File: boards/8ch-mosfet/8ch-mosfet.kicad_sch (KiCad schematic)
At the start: 16 parts, among them J1 N2K, J2 I2C, J3 Screw_Terminal_01x08, J4 Screw_Terminal_01x08, U1 ESP32-DEVKITC, U2 MCP3208, U3 R-78B3.3-2.0

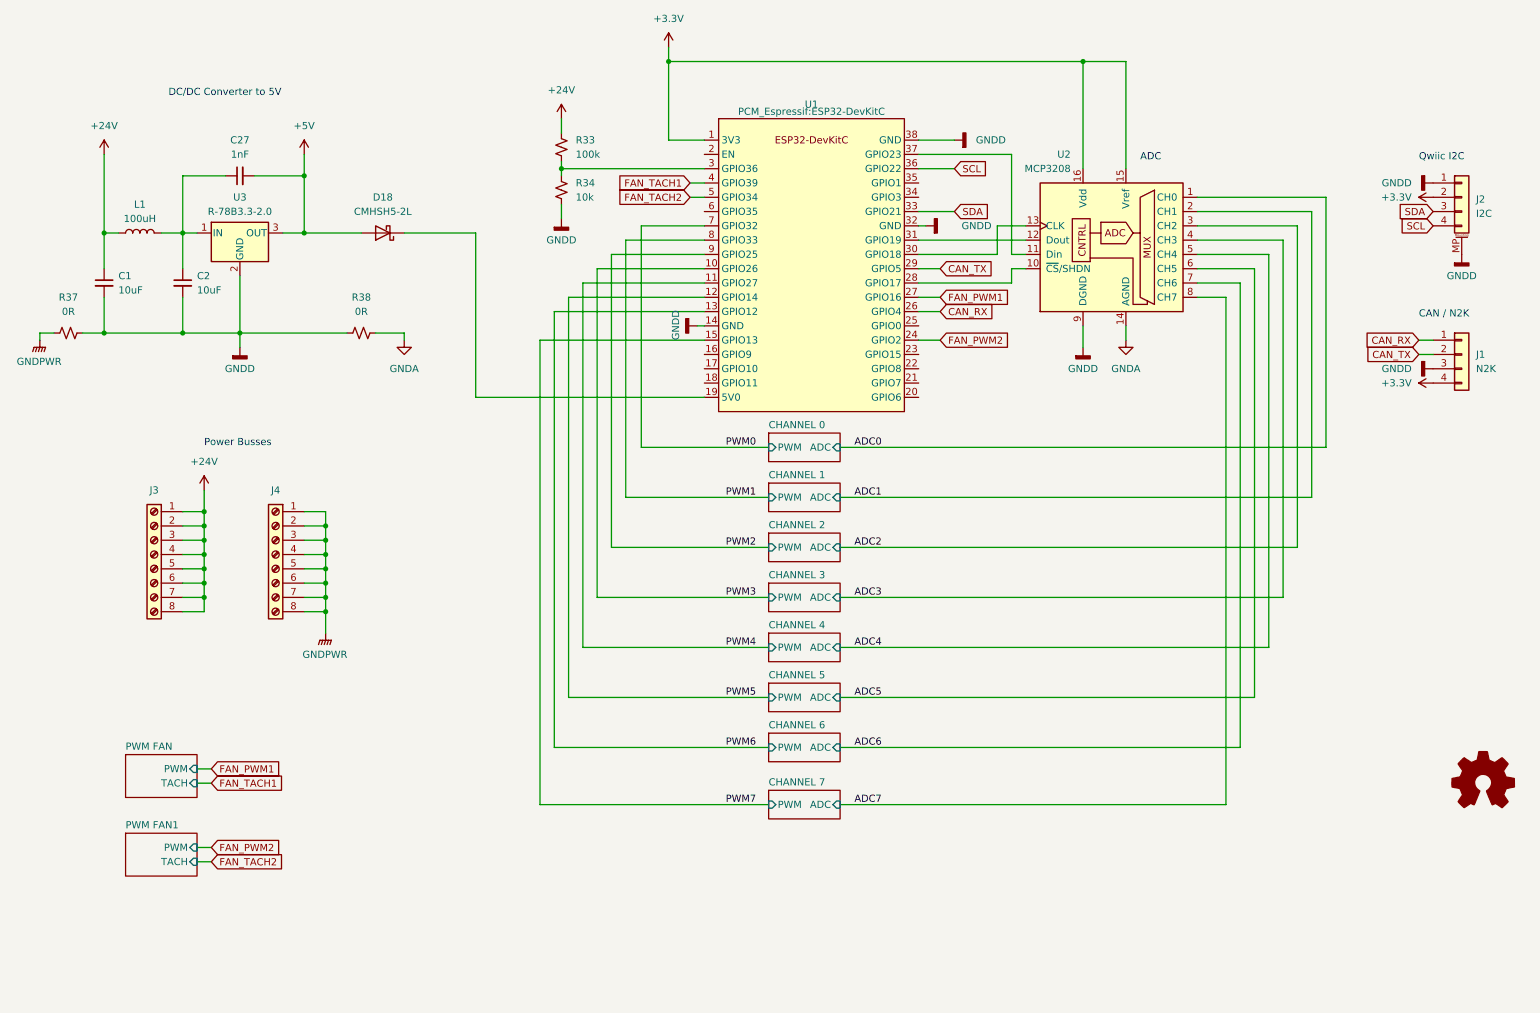
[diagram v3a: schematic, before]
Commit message: added a better adc for getting bus voltage
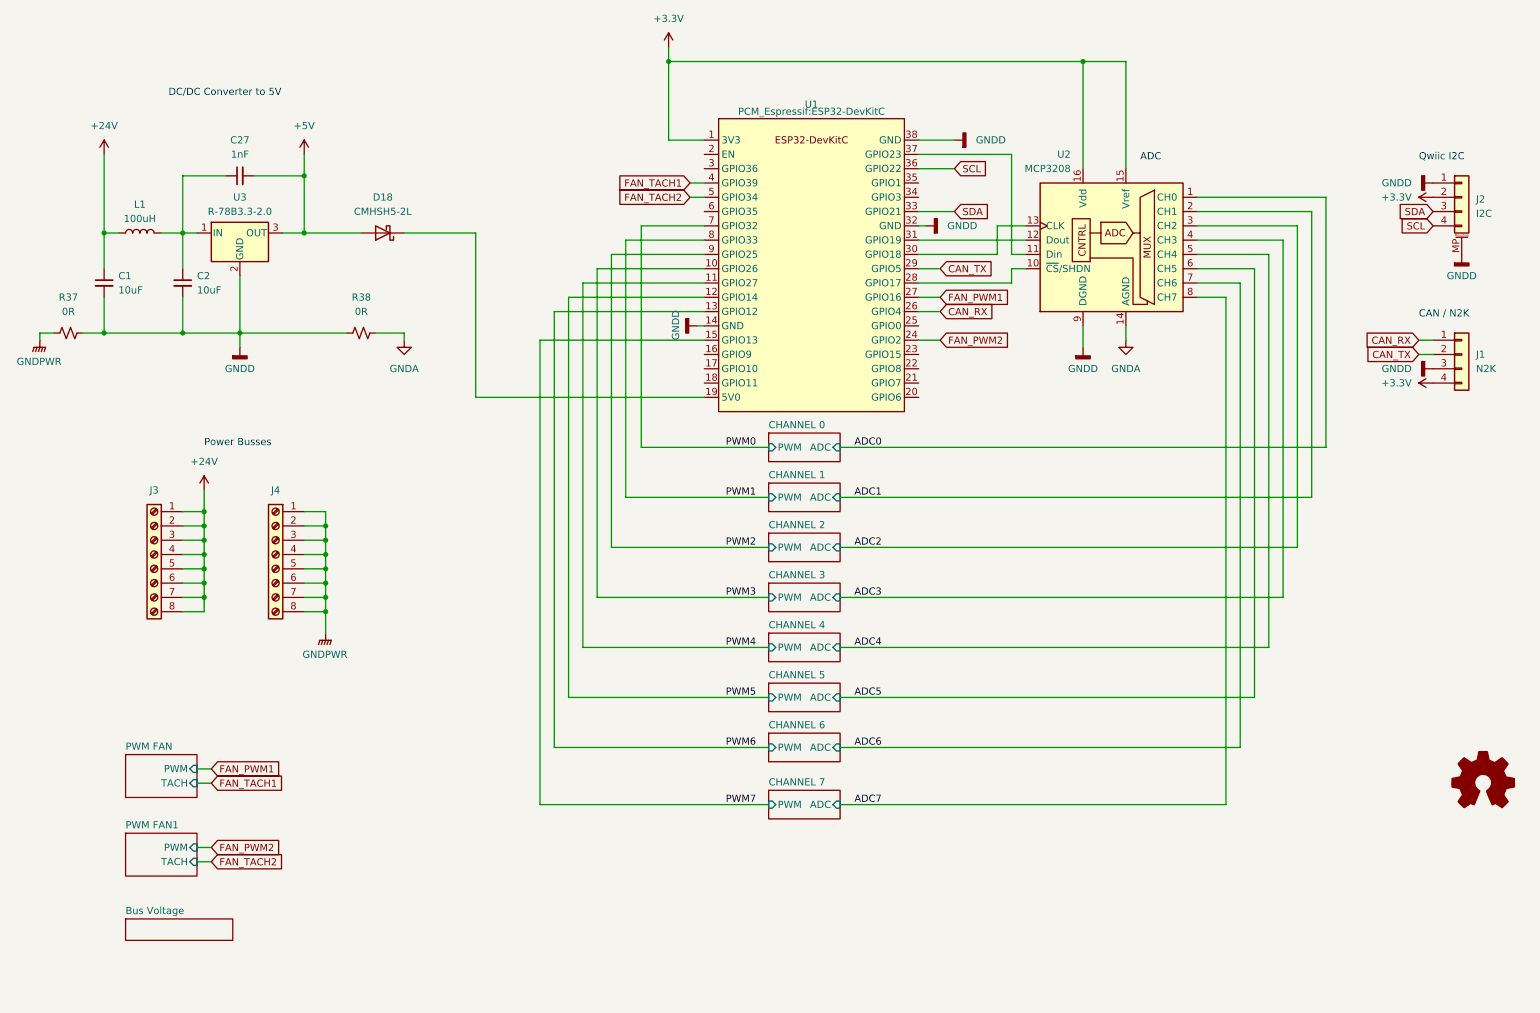
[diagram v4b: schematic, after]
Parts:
- removed R33: 100k, Resistor_SMD:R_0805_2012Metric_Pad1.20x1.40mm_HandSolder, symbol Device:R_Small_US
- removed R34: 10k, Resistor_SMD:R_0805_2012Metric_Pad1.20x1.40mm_HandSolder, symbol Device:R_Small_US
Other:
- added sheet Bus Voltage (bus voltage.kicad_sch)
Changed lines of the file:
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@@
   (junction (at 48.26 110.49) (diameter 0) (color 0 0 0 0)
   )
-  (junction (at 111.76 49.53) (diameter 0) (color 0 0 0 0)
-  )
   (junction (at 48.26 113.03) (diameter 0) (color 0 0 0 0)
   )
@@
     (stroke (width 0) (type default))
   )
-  (wire (pts (xy 111.76 48.26) (xy 111.76 49.53))
-    (stroke (width 0) (type default))
-  )
   (wire (pts (xy 115.57 134.62) (xy 148.59 134.62))
     (stroke (width 0) (type default))
@@
     (stroke (width 0) (type default))
   )
-  (wire (pts (xy 111.76 40.64) (xy 111.76 43.18))
-    (stroke (width 0) (type default))
-  )
   (wire (pts (xy 175.26 44.45) (xy 181.61 44.45))
     (stroke (width 0) (type default))
@@
     (stroke (width 0) (type default))
   )
-  (wire (pts (xy 111.76 49.53) (xy 111.76 50.8))
-    (stroke (width 0) (type default))
-  )
   (wire (pts (xy 48.26 113.03) (xy 48.26 115.57))
     (stroke (width 0) (type default))
@@
     (stroke (width 0) (type default))
   )
-  (wire (pts (xy 111.76 49.53) (xy 137.16 49.53))
-    (stroke (width 0) (type default))
-  )
   (wire (pts (xy 175.26 80.01) (xy 179.07 80.01))
     (stroke (width 0) (type default))
@@
   )
   (wire (pts (xy 204.47 30.48) (xy 204.47 49.53))
-    (stroke (width 0) (type default))
-  )
-  (wire (pts (xy 111.76 55.88) (xy 111.76 58.42))
     (stroke (width 0) (type default))
   )
@@
       (effects (font (size 1.27 1.27)) hide)
     )
-    (property "Value" "GNDD" (at 182.88 59.69 90)
+    (property "Value" "GNDD" (at 180.34 59.69 90)
       (effects (font (size 1.27 1.27)) (justify right))
     )
@@
         (path "/c83c6236-96e9-46ad-9d7a-9e2efa4a7966/a8a81147-5613-4820-beb3-a7ca76d0db8e"
           (reference "R29") (unit 1)
-        )
-      )
-    )
-  )
-  (symbol (lib_id "Device:R_Small_US") (at 111.76 53.34 180) (unit 1)
-    (in_bom yes) (on_board yes) (dnp no) (fields_autoplaced)
-    (property "Reference" "R34" (at 114.3 52.07 0)
-      (effects (font (size 1.27 1.27)) (justify right))
-    )
-    (property "Value" "10k" (at 114.3 54.61 0)
-      (effects (font (size 1.27 1.27)) (justify right))
-    )
-    (property "Footprint" "Resistor_SMD:R_0805_2012Metric_Pad1.20x1.40mm_HandSolder" (at 111.76 53.34 0)
-      (effects (font (size 1.27 1.27)) hide)
-    )
-    (property "Datasheet" "~" (at 111.76 53.34 0)
-      (effects (font (size 1.27 1.27)) hide)
-    )
-    (property "Vendor" "652-CR0805JW-104ELF" (at 111.76 53.34 0)
-      (effects (font (size 1.27 1.27)) hide)
-    )
-    (pin "1")
-    (pin "2")
-    (instances
-      (project "8ch-mosfet"
-        (path "/c83c6236-96e9-46ad-9d7a-9e2efa4a7966"
-          (reference "R34") (unit 1)
-        )
-        (path "/c83c6236-96e9-46ad-9d7a-9e2efa4a7966/0eec6767-666b-42c0-ba36-2a83c9caeade"
-          (reference "R4") (unit 1)
-        )
-        (path "/c83c6236-96e9-46ad-9d7a-9e2efa4a7966/ccdb1c25-8d0f-4f30-ab70-bbc1ecf3f6f7"
-          (reference "R8") (unit 1)
-        )
-        (path "/c83c6236-96e9-46ad-9d7a-9e2efa4a7966/1e692482-a022-407a-8cb5-d9a3b23521a6"
-          (reference "R12") (unit 1)
-        )
-        (path "/c83c6236-96e9-46ad-9d7a-9e2efa4a7966/5952e660-2bb6-45cf-b9ea-f7a7c2d0954e"
-          (reference "R16") (unit 1)
-        )
-        (path "/c83c6236-96e9-46ad-9d7a-9e2efa4a7966/772d44f5-8758-48db-a140-72ed8e75e88c"
-          (reference "R20") (unit 1)
-        )
-        (path "/c83c6236-96e9-46ad-9d7a-9e2efa4a7966/424e7b24-5644-46f2-85bb-1e459a343705"
-          (reference "R24") (unit 1)
-        )
-        (path "/c83c6236-96e9-46ad-9d7a-9e2efa4a7966/4c1df725-56ca-4be4-8107-a39054acbca4"
-          (reference "R28") (unit 1)
-        )
-        (path "/c83c6236-96e9-46ad-9d7a-9e2efa4a7966/a8a81147-5613-4820-beb3-a7ca76d0db8e"
-          (reference "R32") (unit 1)
         )
       )
@@
     )
   )
-  (symbol (lib_id "Device:R_Small_US") (at 111.76 45.72 180) (unit 1)
-    (in_bom yes) (on_board yes) (dnp no) (fields_autoplaced)
-    (property "Reference" "R33" (at 114.3 44.45 0)
-      (effects (font (size 1.27 1.27)) (justify right))
-    )
-    (property "Value" "100k" (at 114.3 46.99 0)
-      (effects (font (size 1.27 1.27)) (justify right))
-    )
-    (property "Footprint" "Resistor_SMD:R_0805_2012Metric_Pad1.20x1.40mm_HandSolder" (at 111.76 45.72 0)
-      (effects (font (size 1.27 1.27)) hide)
-    )
-    (property "Datasheet" "~" (at 111.76 45.72 0)
-      (effects (font (size 1.27 1.27)) hide)
-    )
-    (property "Vendor" "652-CR0805JW-104ELF" (at 111.76 45.72 0)
-      (effects (font (size 1.27 1.27)) hide)
-    )
-    (pin "1")
-    (pin "2")
-    (instances
-      (project "8ch-mosfet"
-        (path "/c83c6236-96e9-46ad-9d7a-9e2efa4a7966"
-          (reference "R33") (unit 1)
-        )
-        (path "/c83c6236-96e9-46ad-9d7a-9e2efa4a7966/0eec6767-666b-42c0-ba36-2a83c9caeade"
-          (reference "R4") (unit 1)
-        )
-        (path "/c83c6236-96e9-46ad-9d7a-9e2efa4a7966/ccdb1c25-8d0f-4f30-ab70-bbc1ecf3f6f7"
-          (reference "R8") (unit 1)
-        )
-        (path "/c83c6236-96e9-46ad-9d7a-9e2efa4a7966/1e692482-a022-407a-8cb5-d9a3b23521a6"
-          (reference "R12") (unit 1)
-        )
-        (path "/c83c6236-96e9-46ad-9d7a-9e2efa4a7966/5952e660-2bb6-45cf-b9ea-f7a7c2d0954e"
-          (reference "R16") (unit 1)
-        )
-        (path "/c83c6236-96e9-46ad-9d7a-9e2efa4a7966/772d44f5-8758-48db-a140-72ed8e75e88c"
-          (reference "R20") (unit 1)
-        )
-        (path "/c83c6236-96e9-46ad-9d7a-9e2efa4a7966/424e7b24-5644-46f2-85bb-1e459a343705"
-          (reference "R24") (unit 1)
-        )
-        (path "/c83c6236-96e9-46ad-9d7a-9e2efa4a7966/4c1df725-56ca-4be4-8107-a39054acbca4"
-          (reference "R28") (unit 1)
-        )
-        (path "/c83c6236-96e9-46ad-9d7a-9e2efa4a7966/a8a81147-5613-4820-beb3-a7ca76d0db8e"
-          (reference "R32") (unit 1)
-        )
-      )
-    )
-  )
   (symbol (lib_id "power:GNDA") (at 83.82 80.01 0) (unit 1)
     (in_bom yes) (on_board yes) (dnp no) (fields_autoplaced)
@@
         (path "/c83c6236-96e9-46ad-9d7a-9e2efa4a7966"
           (reference "D26") (unit 1)
-        )
-      )
-    )
-  )
-  (symbol (lib_id "power:GNDD") (at 111.76 58.42 0) (unit 1)
-    (in_bom yes) (on_board yes) (dnp no) (fields_autoplaced)
-    (property "Reference" "#PWR054" (at 111.76 64.77 0)
-      (effects (font (size 1.27 1.27)) hide)
-    )
-    (property "Value" "GNDD" (at 111.76 62.23 0)
-      (effects (font (size 1.27 1.27)))
-    )
-    (property "Footprint" "" (at 111.76 58.42 0)
-      (effects (font (size 1.27 1.27)) hide)
-    )
-    (property "Datasheet" "" (at 111.76 58.42 0)
-      (effects (font (size 1.27 1.27)) hide)
-    )
-    (pin "1")
-    (instances
-      (project "8ch-mosfet"
-        (path "/c83c6236-96e9-46ad-9d7a-9e2efa4a7966"
-          (reference "#PWR054") (unit 1)
-        )
-      )
-    )
-  )
-  (symbol (lib_id "power:+24V") (at 111.76 40.64 0) (unit 1)
-    (in_bom yes) (on_board yes) (dnp no) (fields_autoplaced)
-    (property "Reference" "#PWR010" (at 111.76 44.45 0)
-      (effects (font (size 1.27 1.27)) hide)
-    )
-    (property "Value" "+24V" (at 111.76 35.56 0)
-      (effects (font (size 1.27 1.27)))
-    )
-    (property "Footprint" "" (at 111.76 40.64 0)
-      (effects (font (size 1.27 1.27)) hide)
-    )
-    (property "Datasheet" "" (at 111.76 40.64 0)
-      (effects (font (size 1.27 1.27)) hide)
-    )
-    (pin "1")
-    (instances
-      (project "8ch-mosfet"
-        (path "/c83c6236-96e9-46ad-9d7a-9e2efa4a7966"
-          (reference "#PWR010") (unit 1)
         )
       )
@@
       )
     )
+  )
+  (sheet (at 34.29 182.88) (size 19.05 3.81) (fields_autoplaced)
+    (stroke (width 0.1524) (type solid))
+    (fill (color 0 0 0 0.0000))
+    (property "Sheetname" "Bus Voltage" (at 34.29 182.1684 0)
+      (effects (font (size 1.27 1.27)) (justify left bottom))
+    )
+    (property "Sheetfile" "bus voltage.kicad_sch" (at 34.29 187.2746 0)
+      (effects (font (size 1.27 1.27)) (justify left top) hide)
+    )
+    (instances
+      (project "8ch-mosfet"
+        (path "/c83c6236-96e9-46ad-9d7a-9e2efa4a7966" (page "12"))
+      )
+    )

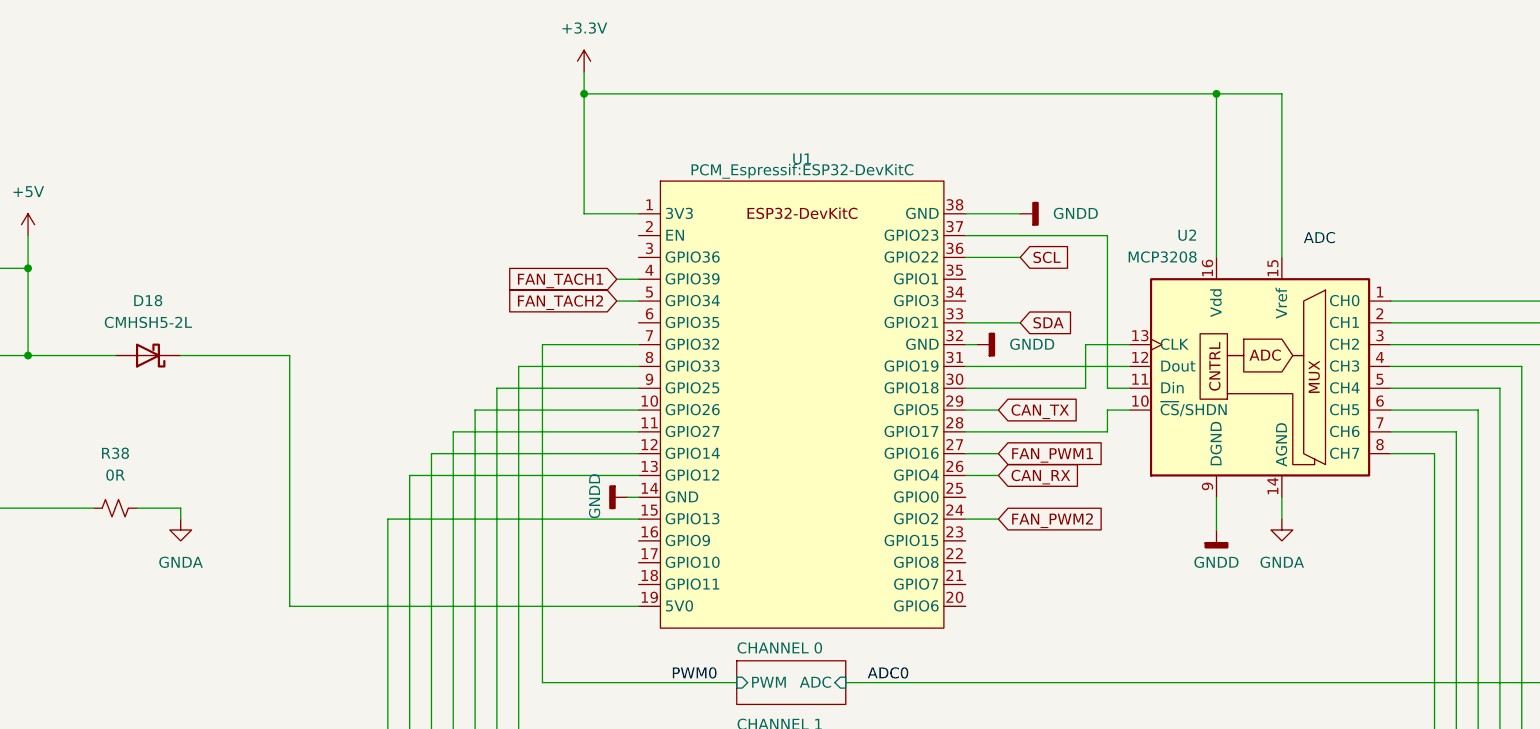
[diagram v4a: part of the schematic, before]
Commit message: updated the adc schematic a bit
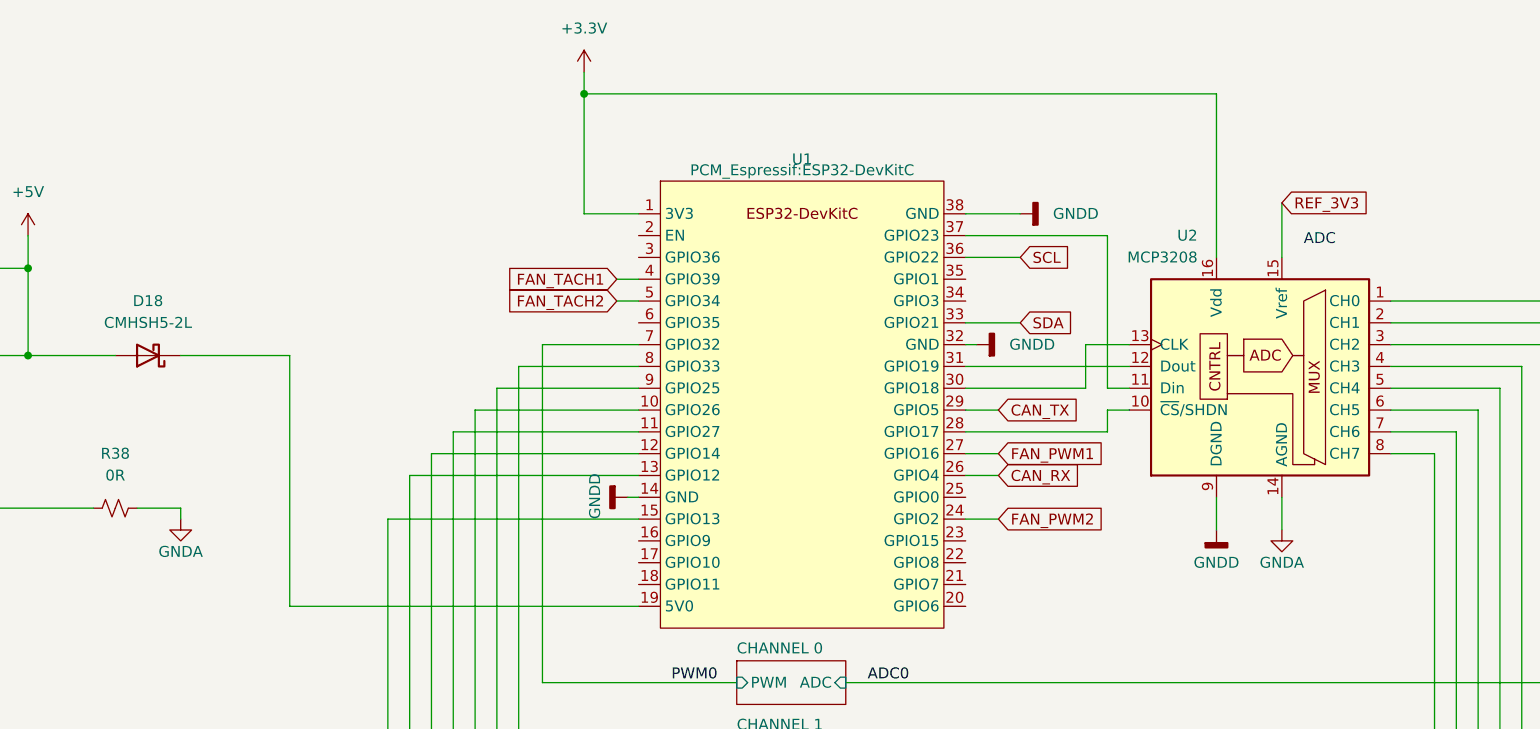
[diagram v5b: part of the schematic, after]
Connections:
- net +3.3V: no longer U2.15 (Vref)
- new net REF_3V3: U2.15 (Vref)
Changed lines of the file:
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@@
   (junction (at 69.85 123.19) (diameter 0) (color 0 0 0 0)
   )
-  (junction (at 204.47 30.48) (diameter 0) (color 0 0 0 0)
-  )
   (junction (at 69.85 120.65) (diameter 0) (color 0 0 0 0)
   )
@@
     (stroke (width 0) (type default))
   )
-  (wire (pts (xy 212.09 30.48) (xy 204.47 30.48))
-    (stroke (width 0) (type default))
-  )
   (wire (pts (xy 224.79 64.77) (xy 237.49 64.77))
     (stroke (width 0) (type default))
@@
     (stroke (width 0) (type default))
   )
-  (wire (pts (xy 212.09 49.53) (xy 212.09 30.48))
-    (stroke (width 0) (type default))
-  )
   (wire (pts (xy 175.26 62.23) (xy 194.31 62.23))
     (stroke (width 0) (type default))
@@
     (stroke (width 0) (type default))
   )
-  (wire (pts (xy 212.09 77.47) (xy 212.09 80.01))
+  (wire (pts (xy 212.09 77.47) (xy 212.09 81.28))
     (stroke (width 0) (type default))
   )
@@
   )
   (wire (pts (xy 115.57 69.85) (xy 115.57 134.62))
+    (stroke (width 0) (type default))
+  )
+  (wire (pts (xy 212.09 43.18) (xy 212.09 49.53))
     (stroke (width 0) (type default))
   )
@@
     (effects (font (size 1.27 1.27)) (justify left))
     (property "Intersheetrefs" "${INTERSHEET_REFS}" (at 62.8567 158.75 0)
+      (effects (font (size 1.27 1.27)) (justify left) hide)
+    )
+  )
+  (global_label "REF_3V3" (shape input) (at 212.09 43.18 0) (fields_autoplaced)
+    (effects (font (size 1.27 1.27)) (justify left))
+    (property "Intersheetrefs" "${INTERSHEET_REFS}" (at 223.058 43.18 0)
       (effects (font (size 1.27 1.27)) (justify left) hide)
     )
@@
     )
   )
-  (symbol (lib_id "power:GNDA") (at 212.09 80.01 0) (unit 1)
-    (in_bom yes) (on_board yes) (dnp no) (fields_autoplaced)
-    (property "Reference" "#PWR07" (at 212.09 86.36 0)
+  (symbol (lib_id "power:GNDA") (at 212.09 81.28 0) (unit 1)
+    (in_bom yes) (on_board yes) (dnp no)
+    (property "Reference" "#PWR07" (at 212.09 87.63 0)
       (effects (font (size 1.27 1.27)) hide)
     )
@@
       (effects (font (size 1.27 1.27)))
     )
-    (property "Footprint" "" (at 212.09 80.01 0)
-      (effects (font (size 1.27 1.27)) hide)
-    )
-    (property "Datasheet" "" (at 212.09 80.01 0)
+    (property "Footprint" "" (at 212.09 81.28 0)
+      (effects (font (size 1.27 1.27)) hide)
+    )
+    (property "Datasheet" "" (at 212.09 81.28 0)
       (effects (font (size 1.27 1.27)) hide)
     )
@@
   )
   (symbol (lib_id "power:GNDA") (at 83.82 80.01 0) (unit 1)
-    (in_bom yes) (on_board yes) (dnp no) (fields_autoplaced)
+    (in_bom yes) (on_board yes) (dnp no)
     (property "Reference" "#PWR055" (at 83.82 86.36 0)
       (effects (font (size 1.27 1.27)) hide)
     )
-    (property "Value" "GNDA" (at 83.82 85.09 0)
-      (effects (font (size 1.27 1.27)))
-    )
+    (property "Value" "GNDA" (at 83.82 83.82 0)
+      (effects (font (size 1.27 1.27)))
+    )
